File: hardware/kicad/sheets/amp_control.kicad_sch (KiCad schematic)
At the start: 10 parts, among them J8 AMP REM / GND, J9 AMP SIGNAL IN / GND, Q5 BSS138, Q6 BSS84

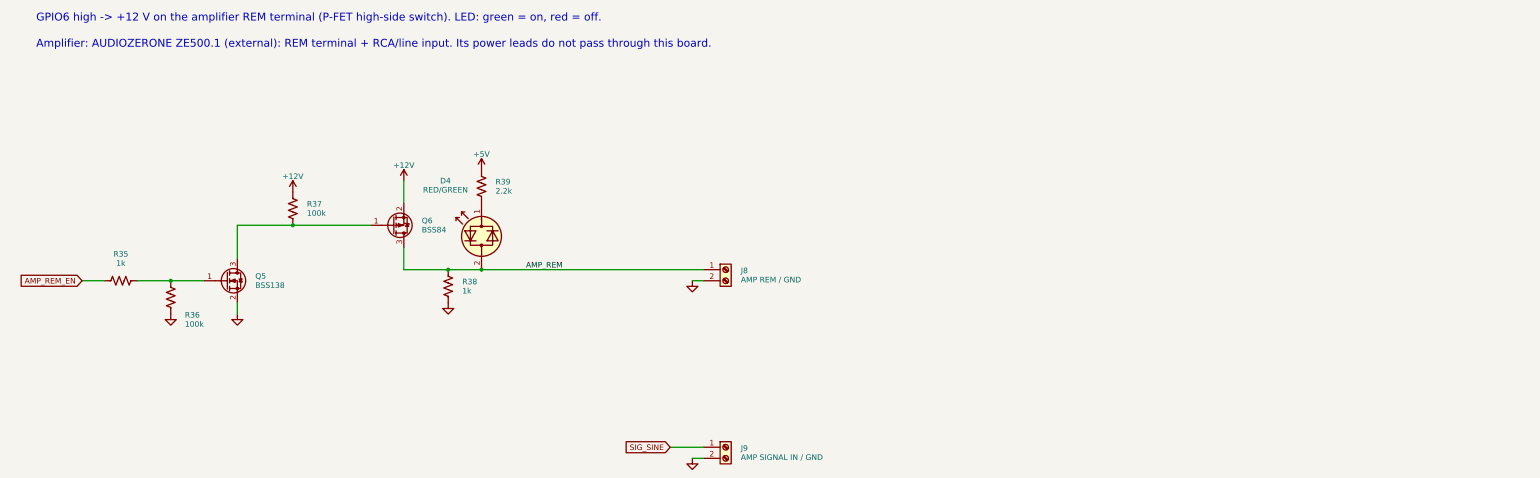
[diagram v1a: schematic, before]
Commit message: Replace the ±15 V LDOs with one LT3097 and add a power-good interlock
- rails_15v: ADP7142 + ADP7182 replaced by one LT3097 (±14.7 V, 147 k SET
  resistors); the ADP5071 output caps are now 22 uF / 50 V and double as the
  LT3097 inputs. PGP / PGN make the PG_15V node (fed from +15 V, so it reads
  0 V if a rail is missing).
- amp_control: a series BSS138 (Q9) gated by PG_15V blocks AMP_REM unless
  both rails are good. New power_good sheet: LED (D23) and the active-low
  PG_15V_N flag on GPIO43 (PG_15V_N_PIN).
- Tooling: LT3097 symbol, footprint and 3D envelope; datasheet rules (191),
  GPIO check, BOM tables, floor plan, PAD_BRIDGES and pre-placed GND vias in
  gen_pcb.py, new fix_route.py for post-route clean-up.
- Board regenerated and routed with Freerouting 2.5.0: DRC 0 unconnected,
  0 schematic-parity issues, no copper violations. Gerbers, JLCPCB zip,
  renders, BOM, CPL and schematic PDF regenerated.

Co-Authored-By: Claude Sonnet 5.5 <noreply@anthropic.com>
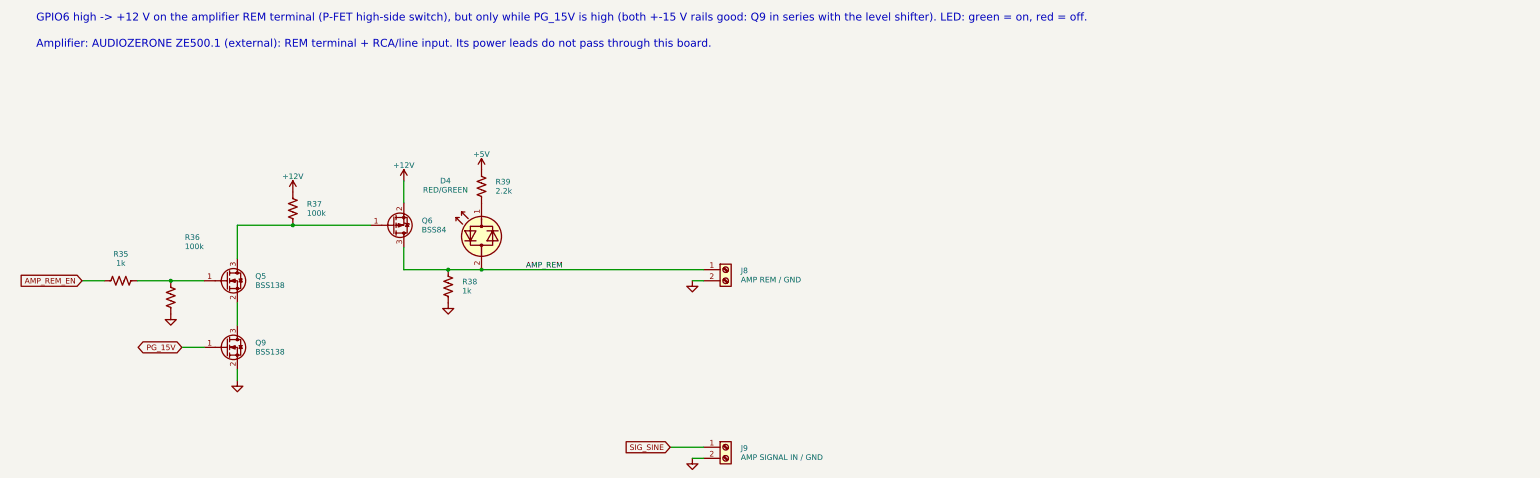
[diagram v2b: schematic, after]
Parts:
- removed D4: RED/GREEN, LED_SMD:LED_1206_3216Metric, symbol Device:LED_Dual_Bidirectional
- added J8: AMP REM / GND, TerminalBlock_Phoenix:TerminalBlock_Phoenix_MKDS-1,5-2-5.08_1x02_P5.08mm_Horizontal, symbol Connector:Screw_Terminal_01x02
- added Q9: BSS138, Package_TO_SOT_SMD:SOT-23, symbol Transistor_FET:BSS138
- D4: renamed from J8; value AMP REM / GND -> RED/GREEN; footprint TerminalBlock_Phoenix:TerminalBlock_Phoenix_MKDS-1,5-2-5.08_1x02_P5.08mm_Horizontal -> LED_SMD:LED_1206_3216Metric; symbol Connector:Screw_Terminal_01x02 -> Device:LED_Dual_Bidirectional
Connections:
- net AMP_REM: now also D4.2 (AK), J8.1 (Pin_1); no longer D4.1 (Pin_1)
- net GND: now also J8.2 (Pin_2), Q9.2 (S); no longer D4.2 (Pin_2), Q5.2 (S)
- net at R39.2: now also D4.1 (KA)
- new net: Q5.2 (S), Q9.3 (D)
- new net PG_15V: Q9.1 (G)
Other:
- note added: "GPIO6 high -> +12 V on the amplifier REM terminal (P-FET high-side switch), but only while PG_15V is high (both +-15 V rails good: Q9 in series with the level shifter). LED: green = on, red = off."
- note removed: "GPIO6 high -> +12 V on the amplifier REM terminal (P-FET high-side switch). LED: green = on, red = off."

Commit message: WIP: restructure PCB for the Phoenix UCS 125-87 housing
Work in progress, layout not finished: about 90 parts still do not fit
their sections and the board is not routed.

- Right-angle connectors: Phoenix MSTBA 2,5 / MC 1,5, JST XH side entry,
  Hirose DF13, Molex 505448-0871 (new footprint from the Molex drawing)
- Datasheet and product links on every symbol (tools/part_links.py)
- Test points so every IC has one on its own nets
- gen_pcb.py: 100 x 62 mm two-sided board, housing holes and restricted
  corners, ESP32 antenna notch, one section per sheet, board ID block,
  ESP32 pin names, pin-1 marks, blue mask
- Housing drawings in hardware/housing/

Co-Authored-By: Claude Opus 5.5 <noreply@anthropic.com>
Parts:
- removed D4: RED/GREEN, LED_SMD:LED_1206_3216Metric, symbol Device:LED_Dual_Bidirectional
- removed R35: 1k, Resistor_SMD:R_0603_1608Metric, symbol Device:R_US
- removed R36: 100k, Resistor_SMD:R_0603_1608Metric, symbol Device:R_US
- removed R39: 2.2k, Resistor_SMD:R_0603_1608Metric, symbol Device:R_US
- added J8: AMP REM / GND, Connector_Phoenix_MC:PhoenixContact_MC_1,5_2-G-3.81_1x02_P3.81mm_Horizontal, symbol Connector:Screw_Terminal_01x02
- added J9: AMP SIGNAL IN / GND, Connector_Phoenix_MC:PhoenixContact_MC_1,5_2-G-3.81_1x02_P3.81mm_Horizontal, symbol Connector:Screw_Terminal_01x02
- added Q9: BSS138, Package_TO_SOT_SMD:SOT-23, symbol Transistor_FET:BSS138
- added R37: 100k, Resistor_SMD:R_0603_1608Metric, symbol Device:R_US
- D4: renamed from J9; value AMP SIGNAL IN / GND -> RED/GREEN; footprint TerminalBlock_Phoenix:TerminalBlock_Phoenix_MKDS-1,5-2-5.08_1x02_P5.08mm_Horizontal -> LED_SMD:LED_1206_3216Metric; symbol Connector:Screw_Terminal_01x02 -> Device:LED_Dual_Bidirectional; Product (none) -> https://www.digikey.com/en/products/result?keywords=XZMDKVG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
- Q5: renamed from R37; value 100k -> BSS138; footprint Resistor_SMD:R_0603_1608Metric -> Package_TO_SOT_SMD:SOT-23; symbol Device:R_US -> Transistor_FET:BSS138; Product (none) -> https://www.digikey.com/en/products/result?keywords=BSS138-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
- Q6: Product (none) -> https://www.digikey.com/en/products/result?keywords=BSS84
- R35: renamed from Q5; value BSS138 -> 1k; footprint Package_TO_SOT_SMD:SOT-23 -> Resistor_SMD:R_0603_1608Metric; symbol Transistor_FET:BSS138 -> Device:R_US; Product (none) -> https://www.digikey.com/en/products/result?keywords=RC0603F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
- R36: renamed from Q9; value BSS138 -> 100k; footprint Package_TO_SOT_SMD:SOT-23 -> Resistor_SMD:R_0603_1608Metric; symbol Transistor_FET:BSS138 -> Device:R_US; Product (none) -> https://www.digikey.com/en/products/result?keywords=AR0603F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
- R38: Product (none) -> https://www.digikey.com/en/products/result?keywords=RC0603F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
- R39: renamed from J8; value AMP REM / GND -> 2.2k; footprint TerminalBlock_Phoenix:TerminalBlock_Phoenix_MKDS-1,5-2-5.08_1x02_P5.08mm_Horizontal -> Resistor_SMD:R_0603_1608Metric; symbol Connector:Screw_Terminal_01x02 -> Device:R_US; Product (none) -> https://www.digikey.com/en/products/result?keywords=RC0603F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
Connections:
- net +12V: now also R37.1; no longer Q5.1
- net +5V: now also R39.1
- net AMP_REM: now also D4.2 (AK), J8.1 (Pin_1); no longer R39.1 (Pin_1)
- net AMP_REM_EN: now also R35.1
- net GND: now also J8.2 (Pin_2), J9.2 (Pin_2), Q9.2 (S); no longer D4.2 (Pin_2), R39.2 (Pin_2)
- net PG_15V: now also Q9.1 (G); no longer R36.1 (G)
- net SIG_SINE: now also J9.1 (Pin_1); no longer D4.1 (Pin_1)
- net at R35.2: now also Q5.1 (G), R36.1; no longer R36.3 (D)
- new net: D4.1 (KA), R39.2
- new net: Q5.3 (D), Q6.1 (G), R37.2
- new net: Q5.2 (S), Q9.3 (D)
